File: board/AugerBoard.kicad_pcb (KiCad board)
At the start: 2 copper layers, 56 parts, among them J1 RJ45_LED_Shielded, Q1 BSS138, Q2 BSS138, Q3 BSS138, SW1 SW_Push, SW10 SW_Push, SW2 SW_Push, SW3 SW_Push, SW4 SW_SPDT, SW5 SW_Push, SW6 SW_Push, SW7 SW_Push, SW8 SW_Push, SW9 SW_Push, U1 OKI-78SR-5_1.5-W36H-C, U2 Teensy4.1_DEV-16771, U3 ATA6561, U6 MAX3485

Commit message: switched soil sensor ports and layout work
soil sensor ports in fact needed to be the way they were originally after looking into the sensors we are using. Also started moving different components on layout to their spots.
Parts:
- removed Conn17: Molex_uF_D_04, MRDT_Connectors:MOLEX_uF_D_04_Horizontal
- added D10: ORANGE, LED_SMD:LED_0603_1608Metric_Pad1.05x0.95mm_HandSolder, F.Cu at (356.7, 153.3)
- added D11: ORANGE, LED_SMD:LED_0603_1608Metric_Pad1.05x0.95mm_HandSolder, F.Cu at (356.7, 155.8)
- added D12: ORANGE, LED_SMD:LED_0603_1608Metric_Pad1.05x0.95mm_HandSolder, F.Cu at (356.7, 158.4)
- added D7: ORANGE, LED_SMD:LED_0603_1608Metric_Pad1.05x0.95mm_HandSolder, F.Cu at (356.7, 145.5)
- added D8: ORANGE, LED_SMD:LED_0603_1608Metric_Pad1.05x0.95mm_HandSolder, F.Cu at (356.7, 148.1)
- added D9: ORANGE, LED_SMD:LED_0603_1608Metric_Pad1.05x0.95mm_HandSolder, F.Cu at (356.7, 150.7)
- added Q4: BSS138, Package_TO_SOT_SMD:SOT-23, F.Cu at (340.1, 146.4)
- added Q5: BSS138, Package_TO_SOT_SMD:SOT-23, F.Cu at (340.1, 150.9)
- added Q6: BSS138, Package_TO_SOT_SMD:SOT-23, F.Cu at (340.1, 155.3)
- added Q7: BSS138, Package_TO_SOT_SMD:SOT-23, F.Cu at (340.1, 159.8)
- added Q8: BSS138, Package_TO_SOT_SMD:SOT-23, F.Cu at (340.1, 164.2)
- added Q9: BSS138, Package_TO_SOT_SMD:SOT-23, F.Cu at (340.1, 168.7)
- added R10: 1.5k, Resistor_SMD:R_0603_1608Metric_Pad0.98x0.95mm_HandSolder, F.Cu at (361.1, 148.0)
- added R11: 1.5k, Resistor_SMD:R_0603_1608Metric_Pad0.98x0.95mm_HandSolder, F.Cu at (361.1, 150.5)
- added R12: 1.5k, Resistor_SMD:R_0603_1608Metric_Pad0.98x0.95mm_HandSolder, F.Cu at (361.1, 153.0)
- added R13: 1.5k, Resistor_SMD:R_0603_1608Metric_Pad0.98x0.95mm_HandSolder, F.Cu at (361.1, 155.5)
- added R14: 1.5k, Resistor_SMD:R_0603_1608Metric_Pad0.98x0.95mm_HandSolder, F.Cu at (361.1, 158.0)
- added R9: 1.5k, Resistor_SMD:R_0603_1608Metric_Pad0.98x0.95mm_HandSolder, F.Cu at (361.1, 145.4)
- added U4: OKI-78SR-3.3_1.5-W36H-C, MRDT_Devices:OKI_Horizontal, F.Cu at (114.3, 73.0)
- Conn16, Conn8: footprint MRDT_Connectors:MOLEX_uF_D_04_Horizontal -> MRDT_Connectors:MOLEX_SL_04_Vertical
- moved Conn7 327.2 mm to (82.1, 135.5)
- moved Conn16 281.8 mm to (125.1, 142.2)
- moved Conn8 272.2 mm to (111.8, 142.2)
- moved Conn2 264.4 mm to (111.8, 119.4)
- moved Conn6 258.9 mm to (113.0, 132.1)
- moved Conn9 257.4 mm to (143.5, 132.1)
- moved Conn3 252.0 mm to (122.6, 119.4)
- moved Conn10 242.5 mm to (128.3, 132.1)
- moved Conn4 239.7 mm to (133.3, 119.4)
- moved C3 228.1 mm to (101.0, 136.5), turned to 90 degrees
- moved Conn5 227.5 mm to (144.1, 119.4)
- moved J1 223.2 mm to (96.5, 162.6)
- moved Conn12 195.7 mm to (138.5, 142.2)
- moved Conn13 186.1 mm to (146.7, 142.2)
- moved H3 123.4 mm to (72.5, 153.6), turned to 180 degrees
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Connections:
- net /Power/SpareLED renamed /Power/SpareMotorLED
- U2 pad 0: unconnected-(U2-RX1-Pad0) -> /Power/AFFLED
- U2 pad 1: unconnected-(U2-TX1-Pad1) -> /Power/AFSpareLED
- U2 pad 17: /Communications/TXD -> unconnected-(U2-A3-Pad17)
- U2 pad 18: /Communications/RXD -> unconnected-(U2-A4-Pad18)
- U2 pad 28: unconnected-(U2-RX7-Pad28) -> /Power/CacheSpareLED
- U2 pad 29: unconnected-(U2-TX7-Pad29) -> /Power/SoilTDLED
- U2 pad 30: unconnected-(U2-CRX3-Pad30) -> /Communications/RXD
- U2 pad 31: unconnected-(U2-CTX3-Pad31) -> /Communications/TXD
- U2 pad 34: unconnected-(U2-RX8-Pad34) -> /Power/SpareServoLED1
- U2 pad 35: unconnected-(U2-TX8-Pad35) -> /Power/SpareServoLED2

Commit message: Layout Progress
Made a basic setup for locations, placed preliminary wires and text, rearranged teensy pins for simplicity
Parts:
- added C4: 10uF, Capacitor_SMD:C_0603_1608Metric_Pad1.08x0.95mm_HandSolder, F.Cu at (114.0, 77.0)
- added C5: 10uF, Capacitor_SMD:C_0603_1608Metric_Pad1.08x0.95mm_HandSolder, F.Cu at (109.0, 77.0)
- added J2: Conn_01x04_MountingPin, Connector_PinHeader_2.54mm:PinHeader_1x04_P2.54mm_Vertical, F.Cu at (155.4, 85.1)
- U1: value OKI-78SR-5_1.5-W36H-C -> OKI 5V
- U4: value OKI-78SR-3.3_1.5-W36H-C -> OKI 3V3
- moved U6 278.5 mm to (126.9, 90.8)
- moved R5 271.0 mm to (132.0, 90.8), turned to 90 degrees
- moved R8 262.1 mm to (87.9, 118.4), turned to -90 degrees
- moved Q3 260.9 mm to (87.9, 126.0), turned to 90 degrees
- moved Q2 258.6 mm to (87.9, 108.2), turned to 90 degrees
- moved R7 258.1 mm to (87.9, 100.6), turned to -90 degrees
- moved Q1 256.9 mm to (87.9, 90.4), turned to 90 degrees
- moved D6 255.1 mm to (87.9, 121.9), turned to 90 degrees
- moved R6 254.9 mm to (87.9, 82.8), turned to -90 degrees
- moved D5 252.8 mm to (87.9, 104.1), turned to 90 degrees
- moved D4 251.4 mm to (87.9, 86.4), turned to 90 degrees
- moved R12 244.3 mm to (118.4, 125.0), turned to 180 degrees
- moved D10 243.6 mm to (114.8, 125.0)
- moved R10 242.9 mm to (118.4, 137.7), turned to 180 degrees
- moved D8 242.2 mm to (114.8, 137.7)
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- renumbered SW4 to SW10, SW5 to SW4, SW6 to SW5, SW7 to SW6, SW8 to SW7, SW9 to SW8, SW10 to SW9
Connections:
- Conn1 pad 4: (no net) -> +12V
- Conn11 pad 4: (no net) -> +12V
- Conn14 pad 4: (no net) -> +12V
- Conn15 pad 4: (no net) -> +12V
- Conn7 pad 4: (no net) -> +12V
- U2 pad 0: /Power/AFFLED -> /Communications/RXD
- U2 pad 1: /Power/AFSpareLED -> /Communications/TXD
- U2 pad 10: /AF interface/AFLED340 -> /AF interface/AFLED490
- U2 pad 11: /AF interface/AFLED490 -> /Power/AFFLED
- U2 pad 12: /AF interface/AFLED405 -> /Servos/AFLensPWM
- U2 pad 13: /Teensy/SoilDoorSW -> /Soil Sensors & NPK/RE
- U2 pad 14: /Teensy/AFLensSW -> /Soil Sensors & NPK/DE
- U2 pad 15: /Teensy/AFSpareSW -> /Soil Sensors & NPK/DI
- U2 pad 16: /Communications/STBY -> /Teensy/SCacheSpareSW
- U2 pad 17: unconnected-(U2-A3-Pad17) -> /Teensy/SoilDoorSW
- U2 pad 18: unconnected-(U2-A4-Pad18) -> /Teensy/GantrySW
- U2 pad 19: /Teensy/GantrySW -> unconnected-(U2-A5-Pad19)
- U2 pad 2: /Servos/SoilTrapdoorPWM -> /Power/SpareMotorLED
- U2 pad 20: /Teensy/AugerSW -> unconnected-(U2-A6-Pad20)
- U2 pad 21: /Teensy/SpareSW_12V -> unconnected-(U2-A7-Pad21)
- U2 pad 22: /Teensy/Dir_Switch -> /Power/VescLED
- U2 pad 23: /Teensy/SCacheSpareSW -> /Power/GantryLED
- U2 pad 24: /Teensy/SpareSW1 -> /Servos/SparePWM1
- U2 pad 25: /Teensy/SpareSW2 -> /Power/SpareServoLED1
- U2 pad 26: /Soil Sensors & NPK/Temp -> /Power/CacheSpareLED
- U2 pad 28: /Power/CacheSpareLED -> /Servos/SoilCacheSparePWM
- U2 pad 29: /Power/SoilTDLED -> /Servos/AFSparePWM
- U2 pad 3: /Servos/AFLensPWM -> /Communications/STBY
- U2 pad 30: /Communications/RXD -> /Power/AFSpareLED
- U2 pad 31: /Communications/TXD -> unconnected-(U2-CTX3-Pad31)
- U2 pad 32: /Power/SpareMotorLED -> unconnected-(U2-OUT1B-Pad32)
- U2 pad 33: unconnected-(U2-MCLK2-Pad33) -> /Teensy/Dir_Switch
- U2 pad 34: /Power/SpareServoLED1 -> /Teensy/SpareSW2
- U2 pad 35: /Power/SpareServoLED2 -> /Teensy/AFSpareSW
- U2 pad 36: unconnected-(U2-CS2-Pad36) -> /Teensy/SpareSW_12V
- U2 pad 37: unconnected-(U2-CS3-Pad37) -> /Teensy/SpareSW1
- U2 pad 38: /Soil Sensors & NPK/RO -> /Soil Sensors & NPK/Temp
- U2 pad 39: /Soil Sensors & NPK/RE -> /Teensy/AFLensSW
- U2 pad 4: /Servos/SoilCacheSparePWM -> /Power/SoilTDLED
- U2 pad 40: /Soil Sensors & NPK/DI -> /Teensy/AugerSW
- U2 pad 41: /Soil Sensors & NPK/DE -> /Soil Sensors & NPK/RO
- U2 pad 5: /Servos/AFSparePWM -> /Servos/SoilTrapdoorPWM
- U2 pad 6: /Servos/SparePWM1 -> /Servos/SparePWM2
- U2 pad 7: /Servos/SparePWM2 -> /Power/SpareServoLED2
- U2 pad 8: /Power/GantryLED -> /AF interface/AFLED340
- U2 pad 9: /Power/VescLED -> /AF interface/AFLED405
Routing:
- net +5V: track 0.00 -> 281.9 mm, vias 0 -> 7
- net +3.3V: track 0.00 -> 183.9 mm, vias 0 -> 6
- net Net-(U3-CANH): track 0.00 -> 97.4 mm, vias 0 -> 3
- net Net-(U3-CANL): track 0.00 -> 96.8 mm, vias 0 -> 2
- net Net-(U6-A): track 0.00 -> 62.4 mm
- net Net-(U6-B): track 0.00 -> 59.4 mm, vias 0 -> 2
- net /Communications/LED: track 0.00 -> 54.6 mm, vias 0 -> 2
- net /Communications/R+: track 0.00 -> 46.8 mm, vias 0 -> 3
- net /Communications/R-: track 0.00 -> 46.8 mm, vias 0 -> 3
- net +12V: track 0.00 -> 46.4 mm, vias 0 -> 3
- net /Teensy/GantrySW: track 0.00 -> 43.5 mm
- net /Teensy/SpareSW_12V: track 0.00 -> 42.9 mm, vias 0 -> 2
- net /Teensy/AugerSW: track 0.00 -> 42.8 mm, vias 0 -> 2
- net /Communications/T+: track 0.00 -> 42.5 mm
- net /Communications/T-: track 0.00 -> 42.4 mm
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- added copper zone on B.Cu, net GND
- added copper zone on F.Cu, net GND
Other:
- board outline added: 96.5 x 99.1 mm
- board text added: "+ -"
- board text added: "+12V"
- board text added: "+3V3"
- board text added: "+5V"
- board text added: "340"
- board text added: "3V3"
- board text added: "405"
- board text added: "490"
- board text added: "5V"
- board text added: "AF LED Signal"
- board text added: "AF Lens"
- board text added: "AF Power"
- board text added: "AF Spare"
- board text added: "Auger"
- board text added: "Auger Gantry"
- board text added: "CAN1"
- board text added: "CAN2"
- board text added: "DIR_SW"
- board text added: "GND"
- board text added: "Gantry Power"
- board text added: "HI"
- board text added: "LO"
- board text added: "Moisture"
- board text added: "NPK & pH"
- board text added: "PWM"
- board text added: "Power In"
- board text added: "SIG"
- board text added: "SW10"
- board text added: "Soil Ch. Spare"
- board text added: "Soil Trapdoor"
- board text added: "Spare"
- board text added: "Spare Anderson"
- board text added: "SpareServo1"
- board text added: "SpareServo2"
- board text added: "Tmp"
- board text added: "UA"
- board text added: "UB"
- board text added: "VESC Power"

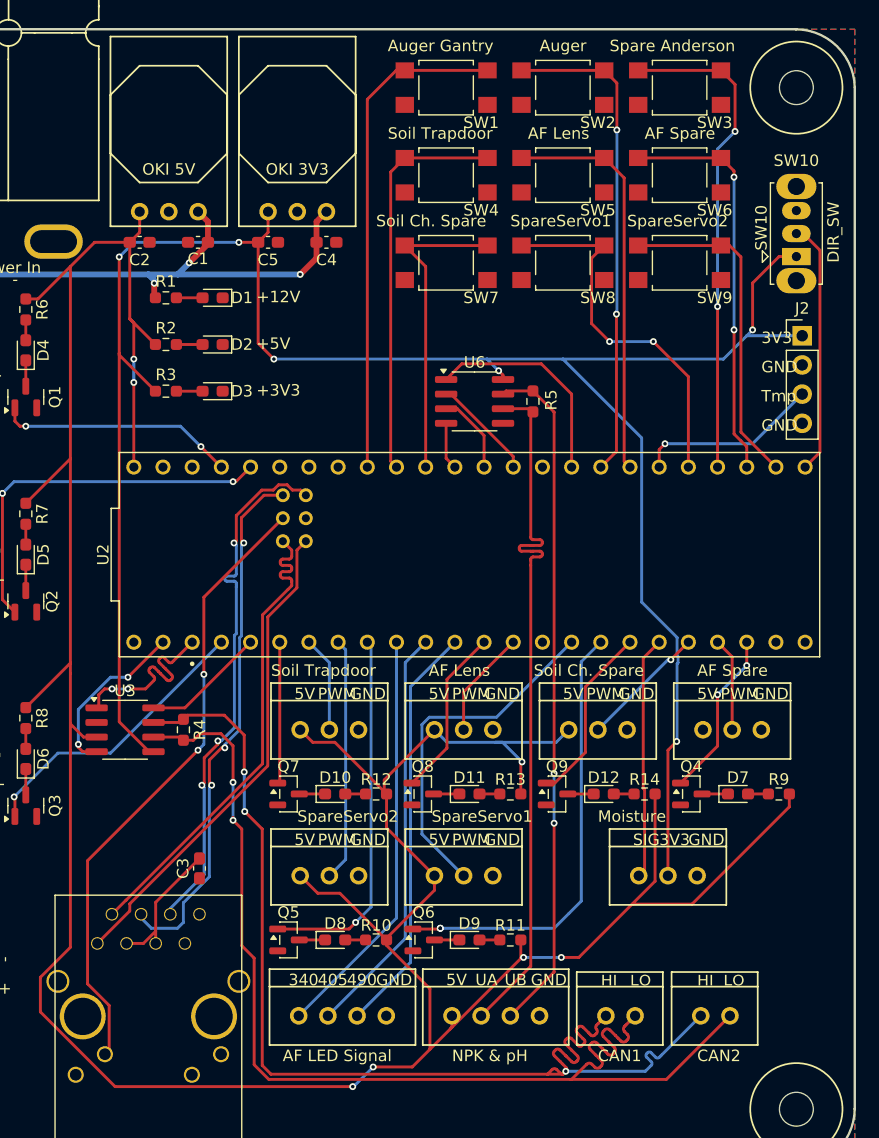
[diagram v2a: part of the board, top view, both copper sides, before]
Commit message: A little refining to the layout
moved wires for clearance
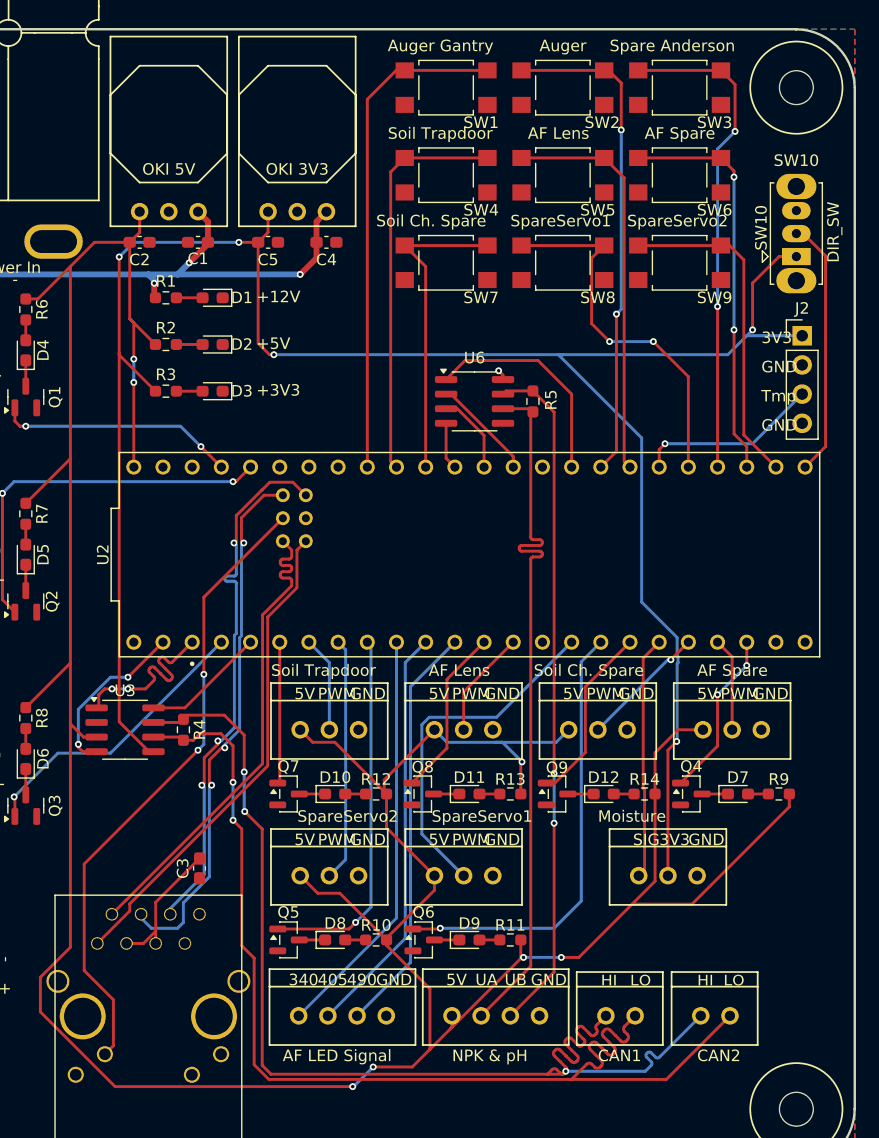
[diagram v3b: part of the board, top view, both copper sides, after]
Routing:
- net +5V: track 281.9 -> 289.8 mm
- net +3.3V: track 183.9 -> 182.5 mm
- net Net-(U3-CANL): track 96.8 -> 95.9 mm
- net Net-(U6-A): track 62.4 -> 61.7 mm
- net +12V: track 46.4 -> 45.8 mm
- net /Teensy/AugerSW: track 42.8 -> 43.3 mm
- net /Servos/SparePWM1: track 31.2 -> 30.7 mm
- net /Power/SpareServoLED1: vias 2 -> 1

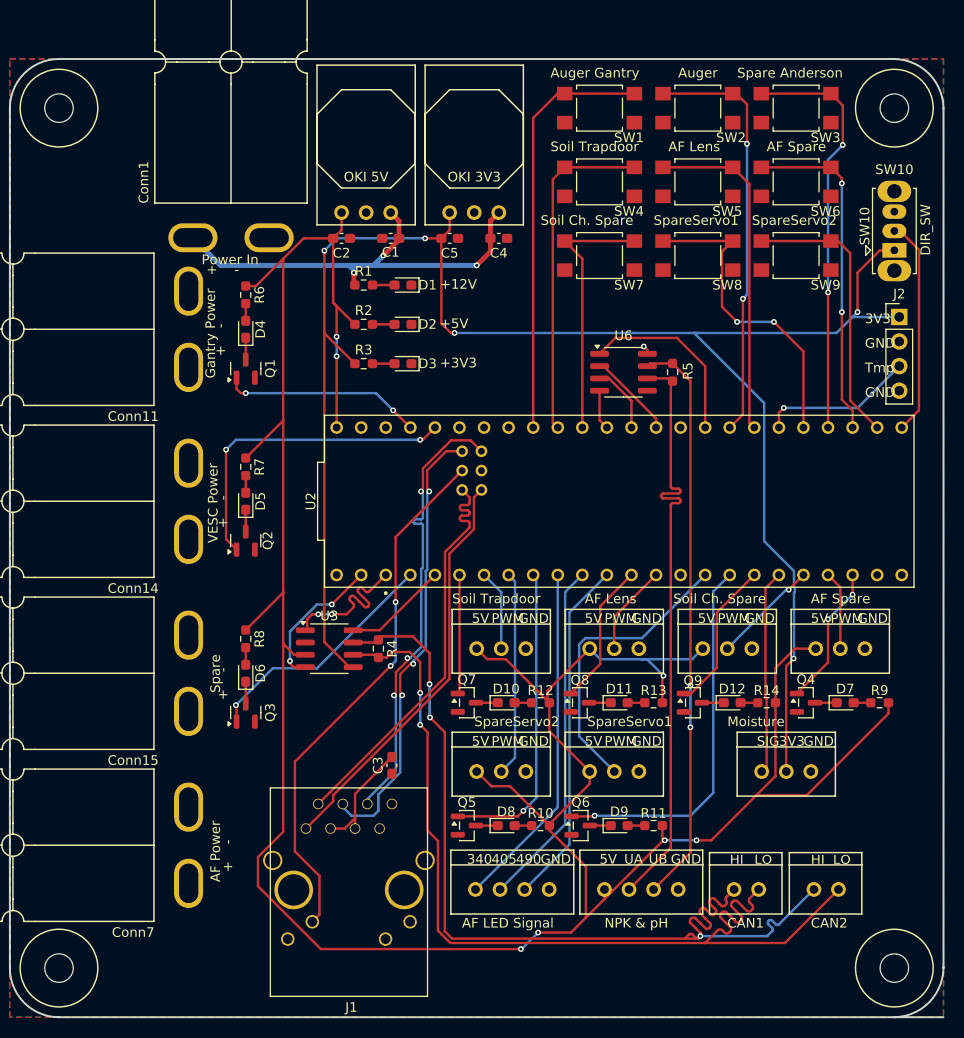
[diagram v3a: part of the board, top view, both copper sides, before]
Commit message: Fixed several errors in the design
Changed font sizes, trace spacing, and added vias for grounding
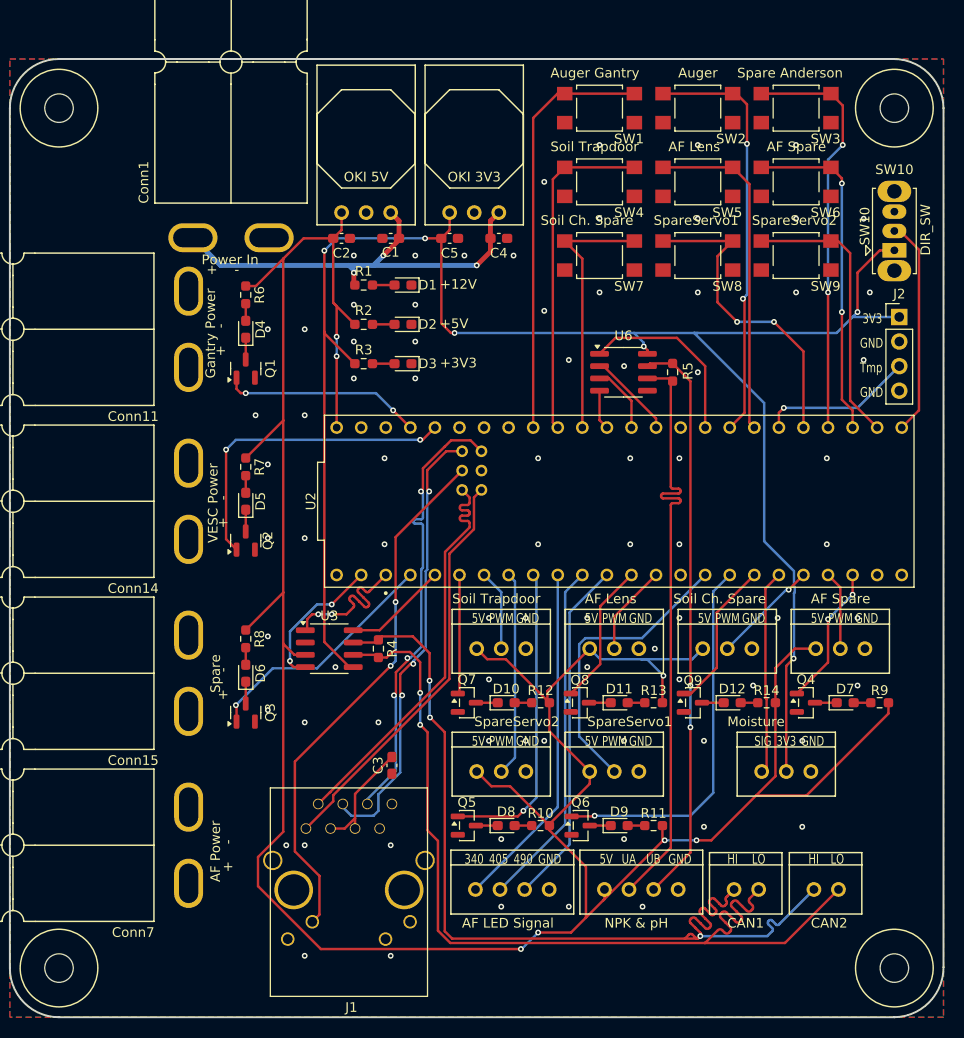
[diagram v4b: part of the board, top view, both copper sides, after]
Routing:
- net +3.3V: track 182.5 -> 184.3 mm
- net GND: vias 0 -> 79
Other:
- outline, holes or cut-outs redrawn
